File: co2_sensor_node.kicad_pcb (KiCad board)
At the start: 4 copper layers, 100 x 100 mm, 122 parts, among them J1 Conn_01x03, J10 Conn_01x04, J11 Conn_01x06_Male, J12 Conn_01x02, J13 TF-15x15, J2 Conn_01x03, J3 Conn_01x02, J4 Conn_01x02, J5 Conn_01x03, J6 Conn_01x03, J7 Conn_01x02, J8 Conn_01x03, J9 Conn_01x04, Q1 AO3400A, Q2 AO3401A, Q3 AO3401A, Q4 AO3400A, SW1 K2-1102SP-C4SC-04, U1 TPS62130, U2 ESP32-WROOM-32D, U3 TC1508S

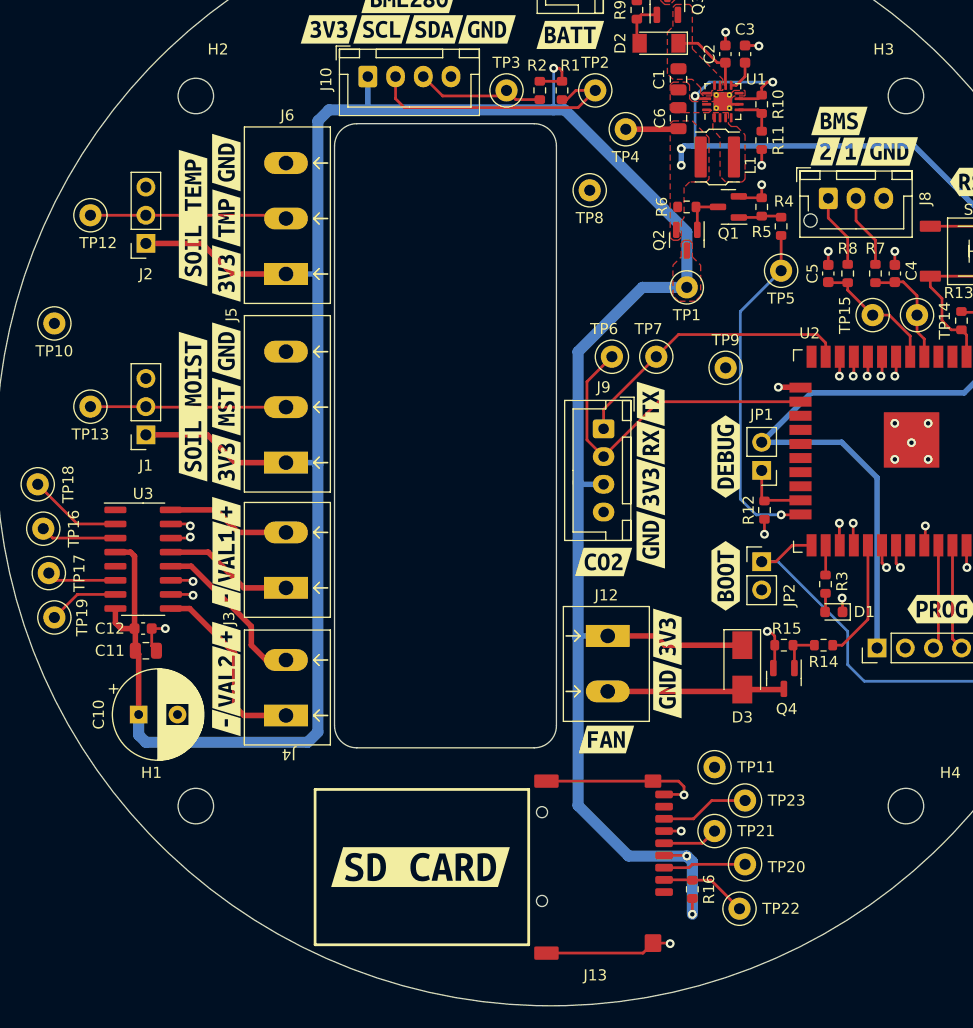
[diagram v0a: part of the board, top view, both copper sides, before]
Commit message: Add voltage selection header for fan
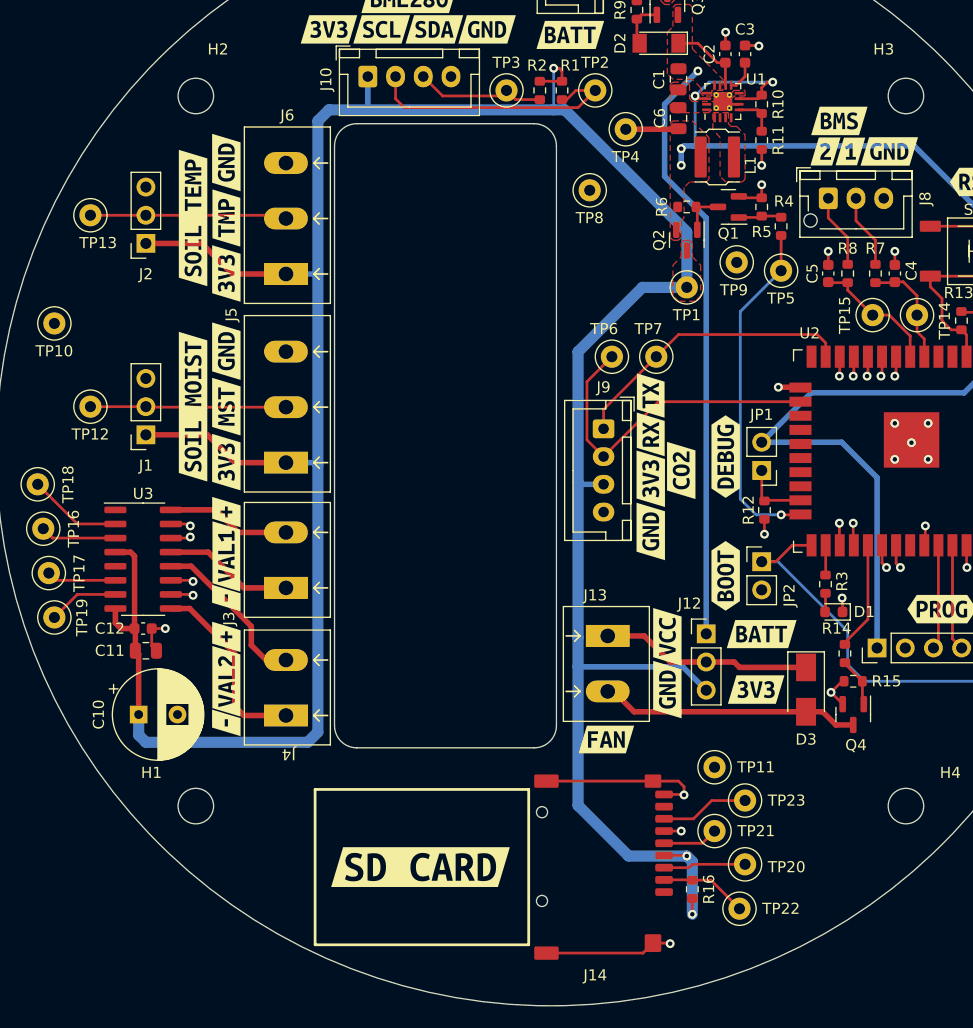
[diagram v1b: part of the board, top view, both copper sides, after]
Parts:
- removed kibuzzard-628D0116: G***, kibuzzard-628D0116
- added J12: Conn_01x03, Connector_PinHeader_2.54mm:PinHeader_1x03_P2.54mm_Vertical, F.Cu at (164.5, 121.5)
- added kibuzzard-6294C7F1: G***, kibuzzard-6294C7F1, F.Cu at (161.0, 121.8)
- added kibuzzard-6294C850: G***, kibuzzard-6294C850, F.Cu at (169.0, 126.5)
- added kibuzzard-6294C860: G***, kibuzzard-6294C860, F.Cu at (169.5, 121.5)
- moved kibuzzard-628D085C 10.8 mm to (162.2, 106.8), turned to 90 degrees
- moved TP9 9.55 mm to (167.2, 88.0)
- moved Q4 7.04 mm to (177.8, 128.8)
- moved R15 7.04 mm to (177.8, 125.8)
- moved D3 6.09 mm to (173.5, 126.5)
- moved R14 2.07 mm to (177.0, 123.2), turned to 90 degrees
- moved kibuzzard-628D0804 0.75 mm to (159.5, 107.5)
- moved kibuzzard-628D0814 0.75 mm to (159.5, 112.2)
- moved kibuzzard-628D0827 0.75 mm to (159.5, 100.0)
- moved kibuzzard-628D082D 0.75 mm to (159.5, 103.5)
- renumbered J12 to J13, J13 to J14, TP13 to TP12, TP12 to TP13
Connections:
- D3 pad 1: /Atmo sensor/3V3_IN -> Net-(D3-Pad1)
- J13 pad 1: /Atmo sensor/3V3_IN -> Net-(D3-Pad1)
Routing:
- net +BATT: track 7.00 -> 60.5 mm, vias 0 -> 1
- net Net-(D3-Pad1): track 0.00 -> 19.0 mm
- net Net-(D3-Pad2): track 16.0 -> 23.4 mm
- net /Atmo sensor/3V3_IN: track 271.6 -> 268.9 mm
- net /Fan/FAN: track 10.9 -> 9.78 mm
- net GND: track 81.3 -> 80.6 mm

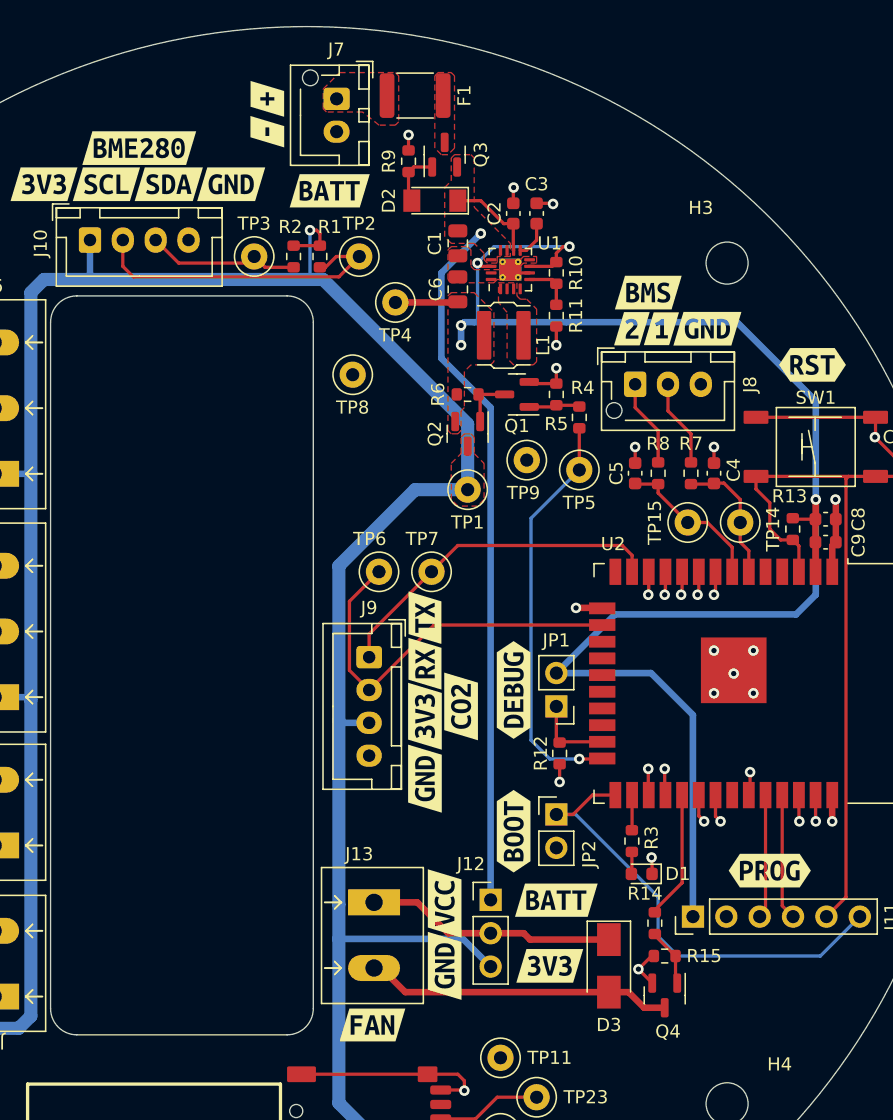
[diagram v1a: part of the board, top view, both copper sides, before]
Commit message: Finalize PCB and generate manufacturing files
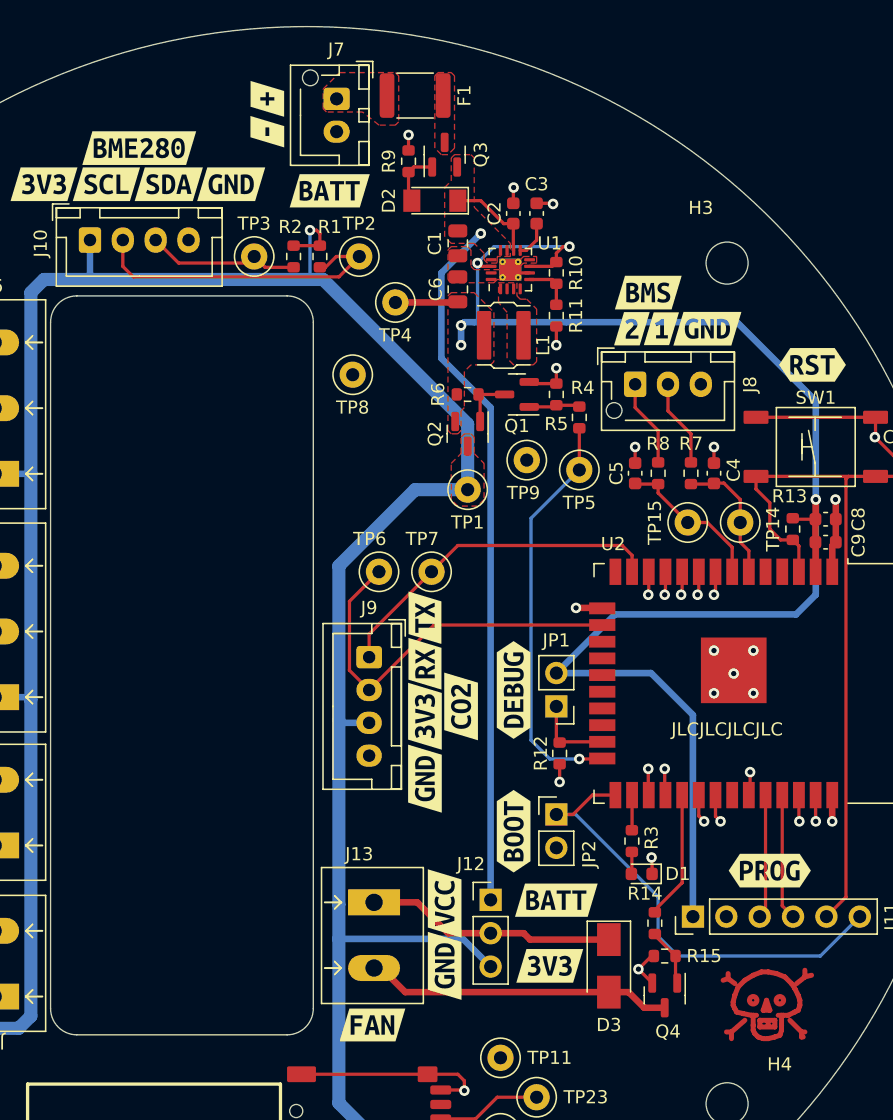
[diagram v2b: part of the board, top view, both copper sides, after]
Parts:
- added REF**: Symbol_Danger_CopperTop_Small, Symbol:Symbol_Danger_CopperTop_Small, F.Cu at (185.5, 129.5)
- added REF**: ESD-Logo_13.2x12mm_SilkScreen, Symbol:ESD-Logo_13.2x12mm_SilkScreen, B.Cu at (174.5, 72.5)
- added kibuzzard-629F6579: G***, kibuzzard-629F6579, B.Cu at (140.8, 134.5)
- added kibuzzard-629F65FE: G***, kibuzzard-629F65FE, B.Cu at (141.2, 141.5)
- added kibuzzard-629F66E0: G***, kibuzzard-629F66E0, B.Cu at (121.5, 101.0)
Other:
- board text added: "JLCJLCJLCJLC"
- board text removed: "HOLE"

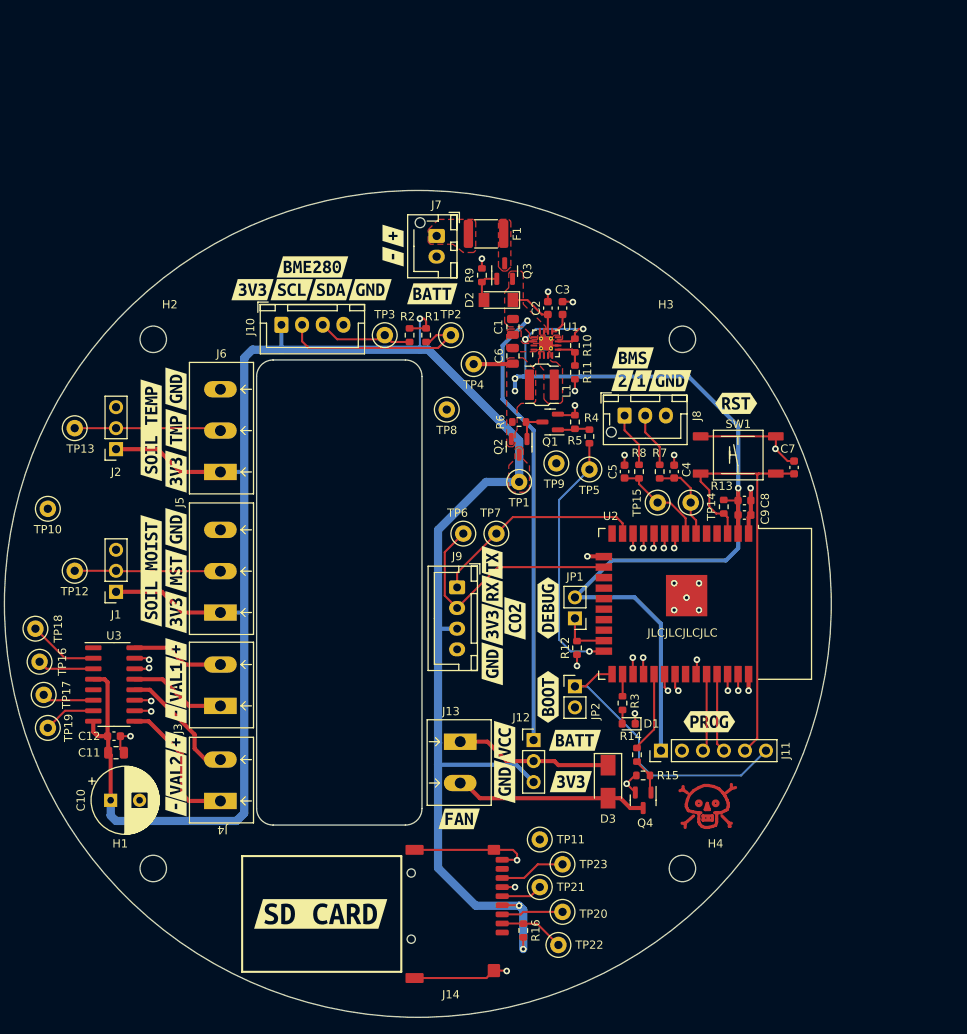
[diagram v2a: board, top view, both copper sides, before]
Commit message: Finish rev. 2 schematic and begin PCB layout
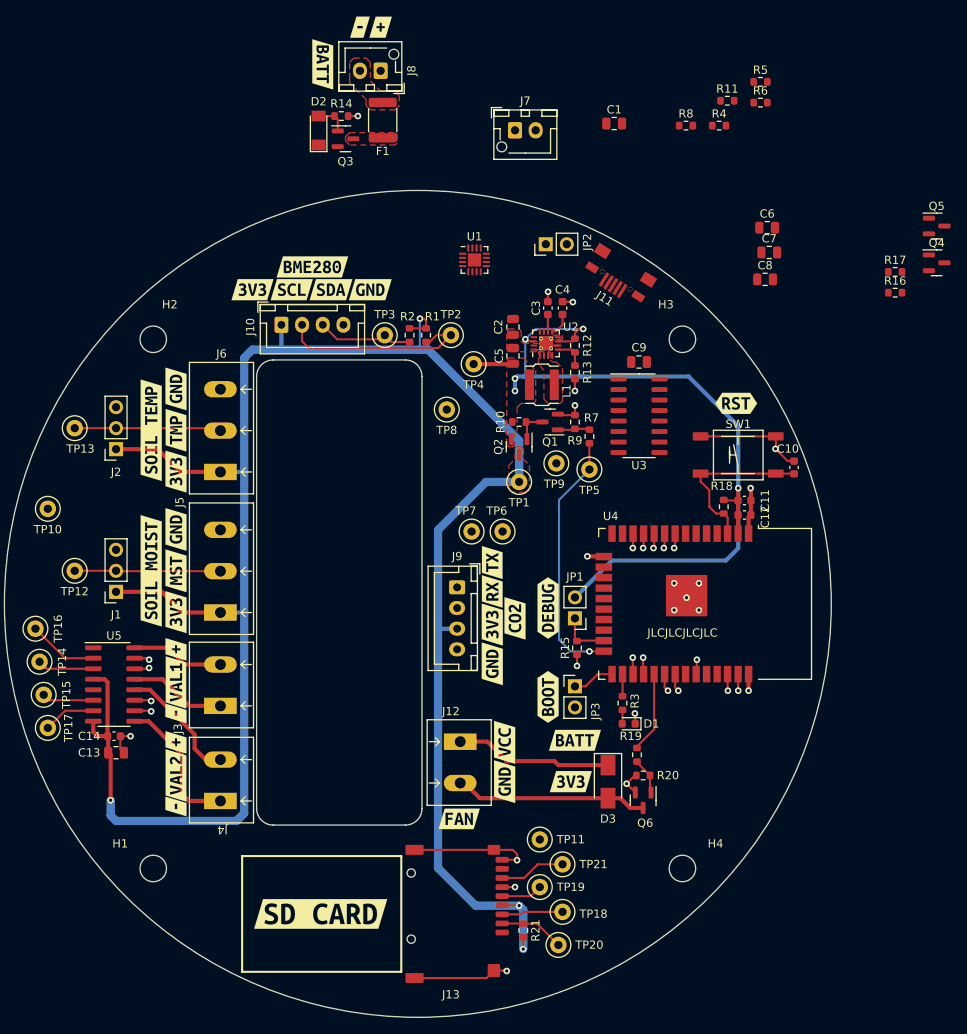
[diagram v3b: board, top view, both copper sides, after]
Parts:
- removed the C10 at (113.3, 128.8)
- removed the C4 at (181.5, 89.0)
- removed the C5 at (175.5, 89.0)
- removed the J12 at (164.5, 121.5)
- removed the J8 at (175.5, 82.2)
- removed the R7 at (179.8, 89.0)
- removed REF**: Symbol_Danger_CopperTop_Small, Symbol:Symbol_Danger_CopperTop_Small
- removed REF**: ESD-Logo_13.2x12mm_SilkScreen, Symbol:ESD-Logo_13.2x12mm_SilkScreen
- removed the TP14 at (183.5, 92.8)
- removed the TP15 at (179.5, 92.8)
- removed kibuzzard-628D019E: G***, kibuzzard-628D019E
- removed kibuzzard-628E05D6: G***, kibuzzard-628E05D6
- removed kibuzzard-628E05DE: G***, kibuzzard-628E05DE
- removed kibuzzard-628E05E8: G***, kibuzzard-628E05E8
- removed kibuzzard-628E05EE: G***, kibuzzard-628E05EE
- added C1: 10u, Capacitor_SMD:C_0805_2012Metric, F.Cu at (174.2, 46.9)
- added C6: 22u, Capacitor_SMD:C_0805_2012Metric, F.Cu at (192.8, 59.5)
- added C7: 22u, Capacitor_SMD:C_0805_2012Metric, F.Cu at (193.0, 62.5)
- added C8: 22u, Capacitor_SMD:C_0805_2012Metric, F.Cu at (192.5, 65.8)
- added C9: 22u, Capacitor_SMD:C_0805_2012Metric, F.Cu at (177.2, 75.8)
- added J7: Conn_01x02, Connector_JST:JST_XH_B2B-XH-AM_1x02_P2.50mm_Vertical, F.Cu at (162.2, 47.7)
- added JP2: USB_PWR_JP, Connector_PinHeader_2.54mm:PinHeader_1x02_P2.54mm_Vertical, F.Cu at (166.0, 61.5)
- added Q4: SS8050, Package_TO_SOT_SMD:SOT-23, F.Cu at (213.2, 63.8)
- added Q5: SS8050, Package_TO_SOT_SMD:SOT-23, F.Cu at (213.2, 59.3)
- added R11: 10k, Resistor_SMD:R_0603_1608Metric, F.Cu at (187.9, 44.1)
- added R16: 12k, Resistor_SMD:R_0603_1608Metric, F.Cu at (208.2, 67.4)
- added R17: 12k, Resistor_SMD:R_0603_1608Metric, F.Cu at (208.2, 64.8)
- added R4: 5k6, Resistor_SMD:R_0603_1608Metric, F.Cu at (186.9, 47.2)
- added R5: 10k, Resistor_SMD:R_0603_1608Metric, F.Cu at (191.9, 41.9)
- added R6: 560, Resistor_SMD:R_0603_1608Metric, F.Cu at (191.9, 44.4)
- added U1: BQ24074RGT, Package_DFN_QFN:VQFN-16-1EP_3x3mm_P0.5mm_EP1.6x1.6mm, F.Cu at (157.3, 63.4)
- added U3: CH340C, Package_SO:SOIC-16_3.9x9.9mm_P1.27mm, F.Cu at (177.2, 82.2)
- J11: value Conn_01x06_Male -> USB_B; footprint Connector_PinHeader_2.54mm:PinHeader_1x06_P2.54mm_Vertical -> co2_sensor_node:USB_MicroQTJ
- R8: value 220 -> 1k5
- TP6: value CO2_RX -> CO2_TX
- TP7: value CO2_TX -> CO2_RX
- moved J11 55.8 mm to (175.2, 67.1), turned to 148 degrees
- moved R8 42.2 mm to (182.9, 47.2), turned to 0 degrees
- moved kibuzzard-628D06EC 30.8 mm to (139.0, 39.8), turned to -90 degrees
- moved D2 29.9 mm to (138.5, 47.8), turned to 90 degrees
- moved kibuzzard-628D076D 28.0 mm to (143.5, 35.2), turned to 0 degrees
- moved R14 25.7 mm to (141.2, 46.0), turned to 0 degrees
- moved kibuzzard-628D0781 25.3 mm to (146.0, 35.2), turned to 0 degrees
- moved Q3 25.0 mm to (141.8, 48.8), turned to 0 degrees
- moved J8 21.1 mm to (146.0, 40.5), turned to 180 degrees
- moved F1 18.6 mm to (146.2, 46.5), turned to 90 degrees
- moved TP6 4.76 mm to (160.8, 96.2)
- moved TP7 3.01 mm to (157.0, 96.2)
- renumbered C7 to C10, C8 to C11, C9 to C12, C11 to C13, C12 to C14, C1 to C2, C2 to C3, C3 to C4, C6 to C5, J13 to J12, J14 to J13, J7 to J8, JP2 to JP3, Q4 to Q6, R6 to R10, R10 to R12, R11 to R13, R9 to R14, R12 to R15, R13 to R18, R14 to R19, R15 to R20, R16 to R21, R4 to R7, R5 to R9, TP16 to TP14, TP17 to TP15, TP18 to TP16, TP19 to TP17, TP20 to TP18, TP21 to TP19, TP22 to TP20, TP23 to TP21, U1 to U2, U2 to U4, U3 to U5
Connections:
- C2 pad 1: +BATT -> /Power/PWR_OUT
- C3 pad 1: +BATT -> /Power/PWR_OUT
- D3 pad 1: Net-(D3-Pad1) -> /Atmo sensor/3V3_IN
- J11 pad 1: +3V3 -> Net-(J11-Pad1)
- J11 pad 2: GND -> Net-(J11-Pad2)
- J11 pad 3: /Microprocessor section/RXD0 -> Net-(J11-Pad3)
- J11 pad 4: /Microprocessor section/TXD0 -> GND
- J11 pad 5: /Microprocessor section/EN -> unconnected-(J11-Pad5)
- J11 pad 6: /Microprocessor section/BOOT -> (no net)
- J12 pad 1: Net-(D3-Pad1) -> /Atmo sensor/3V3_IN
- J8 pad 1: Net-(F1-Pad2) -> GND
- J8 pad 2: GND -> Net-(F1-Pad2)
- R8 pad 1: Net-(J8-Pad1) -> GND
- R8 pad 2: /Microprocessor section/CELL_2 -> Net-(R8-Pad2)
- TP6 pad 1: /CO2 Sensor Connector/UART_RX -> /CO2 Sensor Connector/UART_TX
- TP7 pad 1: /CO2 Sensor Connector/UART_TX -> /CO2 Sensor Connector/UART_RX
- U2 pad 10: +BATT -> /Power/PWR_OUT
- U2 pad 11: +BATT -> /Power/PWR_OUT
- U2 pad 12: +BATT -> /Power/PWR_OUT
- U2 pad 13: +BATT -> /Power/PWR_OUT
- U4 pad 13: /CO2 Sensor Connector/UART_TX -> /CO2 Sensor Connector/UART_RX
- U4 pad 16: /CO2 Sensor Connector/UART_RX -> /CO2 Sensor Connector/UART_TX
- U4 pad 6: /Microprocessor section/CELL_1 -> unconnected-(U4-Pad6)
- U4 pad 7: /Microprocessor section/CELL_2 -> unconnected-(U4-Pad7)
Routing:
- net +BATT: track 60.5 -> 0.00 mm, vias 1 -> 0
- net /Microprocessor section/EN: track 54.7 -> 20.5 mm
- net /Microprocessor section/BOOT: track 35.7 -> 5.11 mm
- net /CO2 Sensor Connector/UART_RX: track 30.3 -> 0.00 mm
- net +3V3: track 124.4 -> 97.3 mm
- net /CO2 Sensor Connector/UART_TX: track 26.1 -> 0.00 mm
- net Net-(D3-Pad1): track 19.0 -> 0.00 mm
- net /Microprocessor section/CELL_2: track 11.7 -> 0.00 mm
- net /Microprocessor section/CELL_1: track 10.1 -> 0.00 mm
- net /Microprocessor section/TXD0: track 9.59 -> 0.00 mm
- net /Microprocessor section/RXD0: track 9.43 -> 0.00 mm
- net Net-(J8-Pad2): track 6.67 -> 0.00 mm
- net Net-(J8-Pad1): track 6.67 -> 0.00 mm
- net /Atmo sensor/3V3_IN: track 268.9 -> 275.5 mm, vias 3 -> 4
- net GND: track 80.6 -> 78.1 mm, vias 27 -> 25
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- removed copper zone on F.Cu, net +BATT

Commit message: Continued PCB layout
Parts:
- moved TP8 52.3 mm to (206.2, 82.5)
- moved TP4 43.2 mm to (168.5, 34.2)
- moved D2 19.6 mm to (126.5, 32.3)
- moved F1 19.6 mm to (134.2, 31.0)
- moved J8 19.6 mm to (134.0, 25.0)
- moved Q3 19.6 mm to (129.7, 33.3)
- moved R14 19.6 mm to (129.2, 30.5)
- moved kibuzzard-628D06EC 19.6 mm to (127.0, 24.3)
- moved kibuzzard-628D076D 19.6 mm to (131.5, 19.8)
- moved kibuzzard-628D0781 19.6 mm to (134.0, 19.8)
- moved TP6 7.22 mm to (167.8, 98.0)
- moved TP7 7.22 mm to (164.0, 98.0)
- moved U1 4.47 mm to (160.2, 60.0)
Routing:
- net +3V3: track 97.3 -> 92.6 mm
